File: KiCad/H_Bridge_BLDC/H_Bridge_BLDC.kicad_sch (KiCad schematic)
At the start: 32 parts, among them J1 DriveCoil, Q1 BC32740BU, Q2 TIP2955G, Q3 TIP3055G, Q4 TIP3055G, Q5 TIP2955G, Q6 BC32740BU, U1 VO615A, U4 VO615A

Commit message: First version
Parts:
- removed D1: GBU6B, Diode_THT:Diode_Bridge_Vishay_GBU, symbol Diode_Bridge:GBU6B
- added D20, D21, D22, D23: 1N5408, Diode_THT:D_DO-201AD_P15.24mm_Horizontal, symbol Diode:1N5408
- C3: footprint Capacitor_THT:CP_Radial_D25.0mm_P10.00mm_SnapIn -> Capacitor_THT:CP_Radial_D10.0mm_P5.00mm; symbol Components:470-uF-250V-PK2E471MND2535 -> Components:470-uF-50V-ECA-1HM471; Digikey https://www.digikey.nl/short/3fbd49pc -> https://www.digikey.nl/short/nq94djb8
- C4, C5, C6: footprint footprints:CP_Radial_D25.0mm_P10.00mm_and_5mm -> Capacitor_THT:CP_Radial_D10.0mm_P5.00mm; symbol Components:470-uF-250V-PK2E471MND2535 -> Components:470-uF-50V-ECA-1HM471; Digikey https://www.digikey.nl/short/3fbd49pc -> https://www.digikey.nl/short/nq94djb8
- Q1, Q6: value BC32740BU -> 2N5401; symbol Components:BC32740BU -> Components:2N5401; Digikey https://www.digikey.nl/short/7rn09zn2 -> https://www.digikey.nl/short/hrnt4cb2
- Q2, Q5: value TIP2955G -> BDW94C; footprint Package_TO_SOT_THT:TO-247-3_Vertical -> Package_TO_SOT_THT:TO-220-3_Vertical; symbol Transistor_BJT:TIP2955G -> Transistor_BJT:BDW94C
- Q3, Q4: value TIP3055G -> BDW93C; footprint Package_TO_SOT_THT:TO-247-3_Vertical -> Package_TO_SOT_THT:TO-220-3_Vertical; symbol Transistor_BJT:TIP3055G -> Transistor_BJT:BDW93C
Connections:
- net BR+: now also D21.1 (K), D23.1 (K)
- net C1: now also D22.1 (K), D23.2 (A)
- net C2: now also D20.1 (K), D21.2 (A)
- net GND: now also D20.2 (A), D22.2 (A)
- net at R3.1: now also Q1.1 (E); no longer Q1.3 (E)
- net at R8.2: now also Q6.1 (E); no longer Q6.3 (E)
- net at Q4.1 (B), R6.1: now also Q6.3 (C); no longer Q6.1 (C)
- net at Q3.1 (B), R5.2: now also Q1.3 (C); no longer Q1.1 (C)

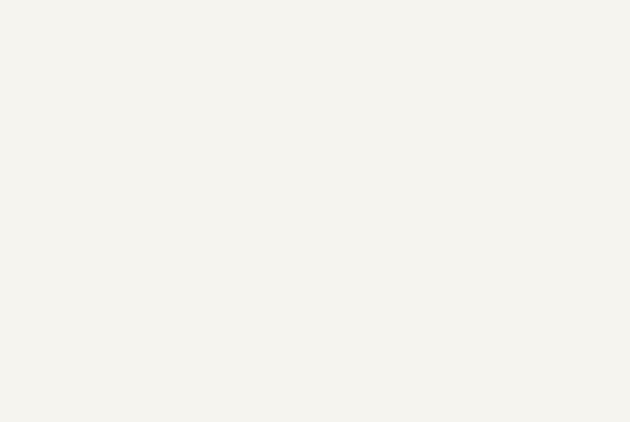
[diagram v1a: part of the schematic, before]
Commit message: Added mounting holes
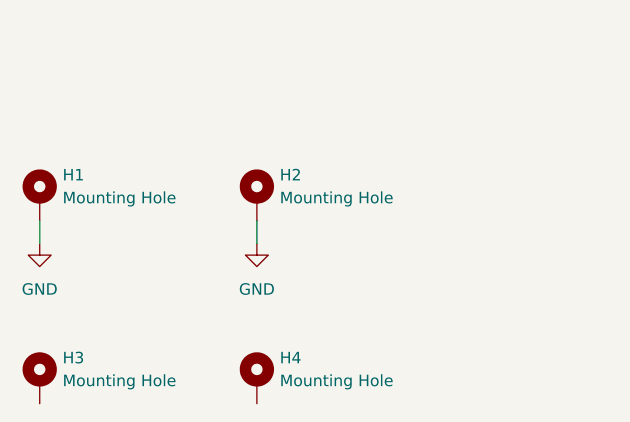
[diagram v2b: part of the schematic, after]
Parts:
- added H1, H2, H3, H4: Mounting Hole, MountingHole:MountingHole_3.2mm_M3_DIN965_Pad, symbol Mechanical:MountingHole_Pad
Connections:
- net GND: now also H1.1, H2.1

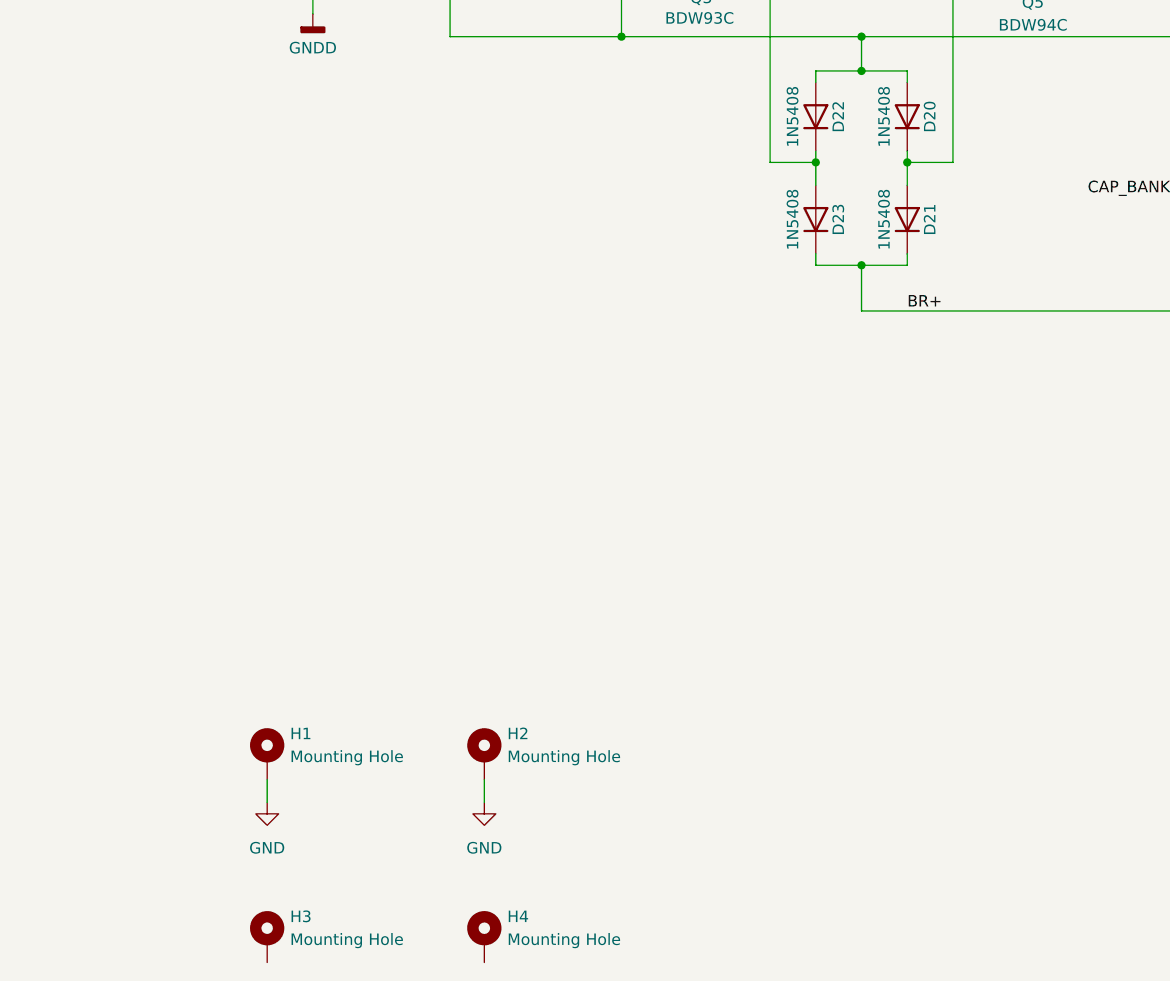
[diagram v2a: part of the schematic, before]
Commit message: Added some connectors for expermental area
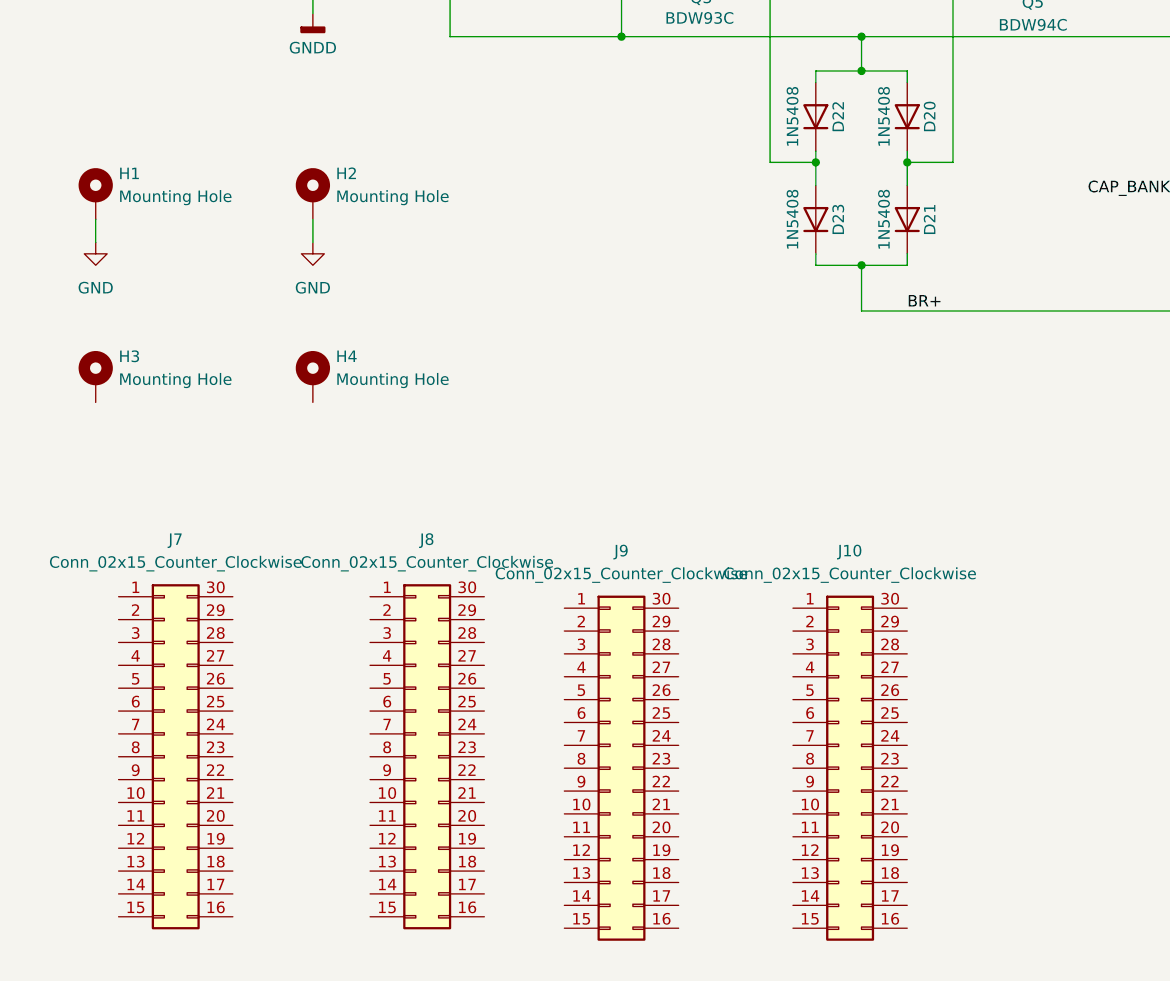
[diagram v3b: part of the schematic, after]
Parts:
- added J10, J7, J8, J9: Conn_02x15_Counter_Clockwise, Connector_PinHeader_2.54mm:PinHeader_2x15_P2.54mm_Vertical, symbol Connector_Generic:Conn_02x15_Counter_Clockwise
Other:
- moved on the sheet: H1, H2, H3, H4

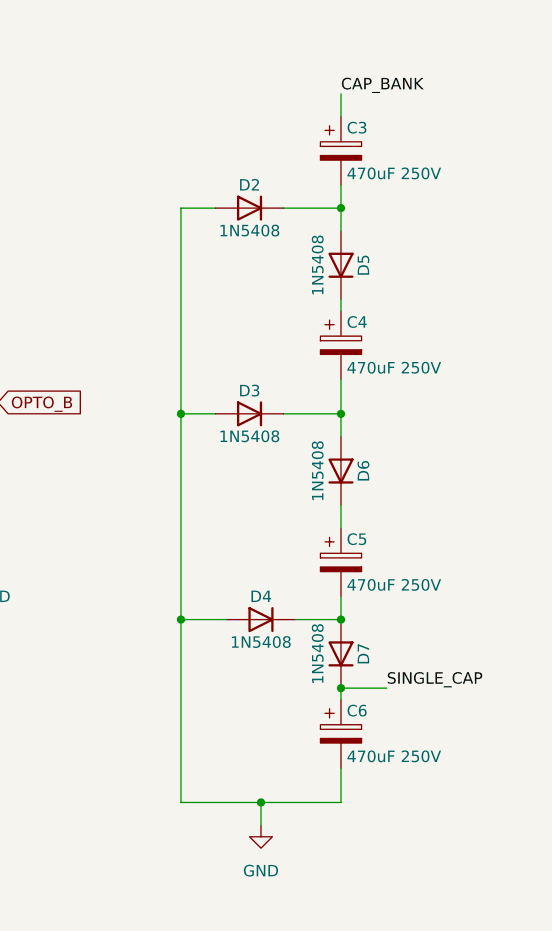
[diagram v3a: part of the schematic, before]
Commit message: Added BOM and changed some parts (same footprint)
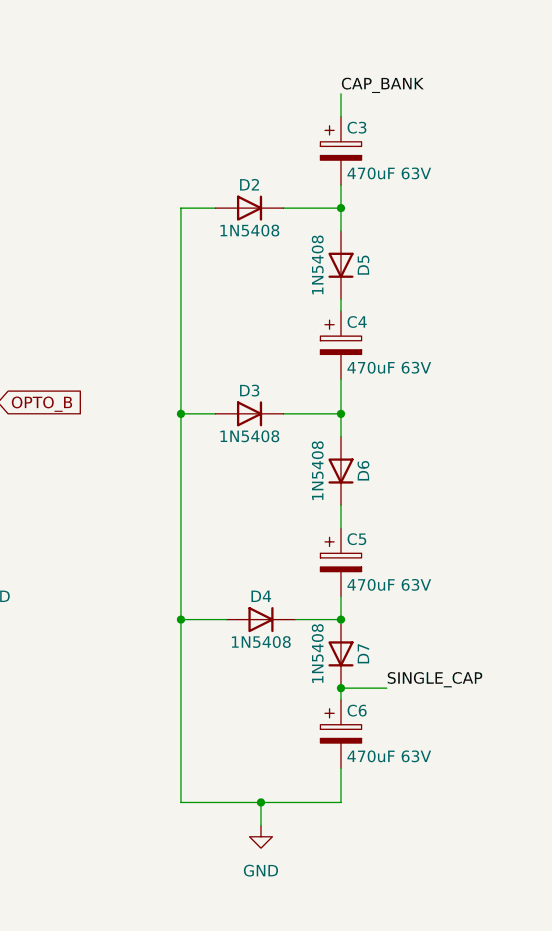
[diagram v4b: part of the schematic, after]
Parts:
- C3, C4, C5, C6: value 470uF 250V -> 470uF 63V; symbol Components:470-uF-50V-ECA-1HM471 -> Components:470-uF-63V-ESK477M063AL4EA; Digikey https://www.digikey.nl/short/nq94djb8 -> https://www.digikey.nl/short/2thtjq03
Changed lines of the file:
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@@
 	)
 	(symbol
-		(lib_id "Components:470-uF-50V-ECA-1HM471")
+		(lib_id "Components:470-uF-63V-ESK477M063AL4EA")
 		(at 220.98 54.61 0)
 		(unit 1)
@@
 			)
 		)
-		(property "Value" "470uF 250V"
+		(property "Value" "470uF 63V"
 			(at 221.615 57.15 0)
 			(effects
@@
 			)
 		)
-		(property "Datasheet" "https://mm.digikey.com/Volume0/opasdata/d220001/medias/docus/2452/ECA-xxM%20Series%2CTypeA.pdf"
+		(property "Datasheet" "https://search.kemet.com/download/datasheet/ESK477M063AL4EA"
 			(at 220.98 54.61 0)
 			(effects
@@
 			)
 		)
-		(property "Digikey" "https://www.digikey.nl/short/nq94djb8"
+		(property "Digikey" "https://www.digikey.nl/short/2thtjq03"
 			(at 220.98 54.61 0)
 			(effects
@@
 	)
 	(symbol
-		(lib_id "Components:470-uF-50V-ECA-1HM471")
+		(lib_id "Components:470-uF-63V-ESK477M063AL4EA")
 		(at 220.98 78.74 0)
 		(unit 1)
@@
 			)
 		)
-		(property "Value" "470uF 250V"
+		(property "Value" "470uF 63V"
 			(at 221.615 81.28 0)
 			(effects
@@
 			)
 		)
-		(property "Datasheet" "https://mm.digikey.com/Volume0/opasdata/d220001/medias/docus/2452/ECA-xxM%20Series%2CTypeA.pdf"
+		(property "Datasheet" "https://search.kemet.com/download/datasheet/ESK477M063AL4EA"
 			(at 220.98 78.74 0)
 			(effects
@@
 			)
 		)
-		(property "Digikey" "https://www.digikey.nl/short/nq94djb8"
+		(property "Digikey" "https://www.digikey.nl/short/2thtjq03"
 			(at 220.98 78.74 0)
 			(effects
@@
 	)
 	(symbol
-		(lib_id "Components:470-uF-50V-ECA-1HM471")
+		(lib_id "Components:470-uF-63V-ESK477M063AL4EA")
 		(at 220.98 97.79 0)
 		(unit 1)
@@
 			)
 		)
-		(property "Value" "470uF 250V"
+		(property "Value" "470uF 63V"
 			(at 221.615 100.33 0)
 			(effects
@@
 			)
 		)
-		(property "Datasheet" "https://mm.digikey.com/Volume0/opasdata/d220001/medias/docus/2452/ECA-xxM%20Series%2CTypeA.pdf"
+		(property "Datasheet" "https://search.kemet.com/download/datasheet/ESK477M063AL4EA"
 			(at 220.98 97.79 0)
 			(effects
@@
 			)
 		)
-		(property "Digikey" "https://www.digikey.nl/short/nq94djb8"
+		(property "Digikey" "https://www.digikey.nl/short/2thtjq03"
 			(at 220.98 97.79 0)
 			(effects
@@
 	)
 	(symbol
-		(lib_id "Components:470-uF-50V-ECA-1HM471")
+		(lib_id "Components:470-uF-63V-ESK477M063AL4EA")
 		(at 220.98 33.02 0)
 		(unit 1)
@@
 			)
 		)
-		(property "Value" "470uF 250V"
+		(property "Value" "470uF 63V"
 			(at 221.615 35.56 0)
 			(effects
@@
 			)
 		)
-		(property "Datasheet" "https://mm.digikey.com/Volume0/opasdata/d220001/medias/docus/2452/ECA-xxM%20Series%2CTypeA.pdf"
+		(property "Datasheet" "https://search.kemet.com/download/datasheet/ESK477M063AL4EA"
 			(at 220.98 33.02 0)
 			(effects
@@
 			)
 		)
-		(property "Digikey" "https://www.digikey.nl/short/nq94djb8"
+		(property "Digikey" "https://www.digikey.nl/short/2thtjq03"
 			(at 220.98 33.02 0)
 			(effects

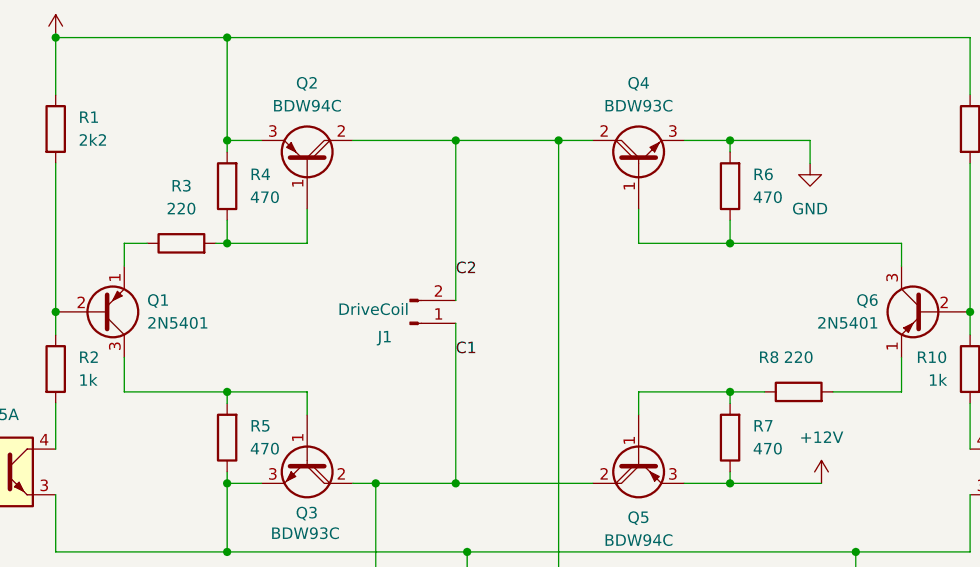
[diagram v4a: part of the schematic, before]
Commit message: Changed a few values and completed BOM.
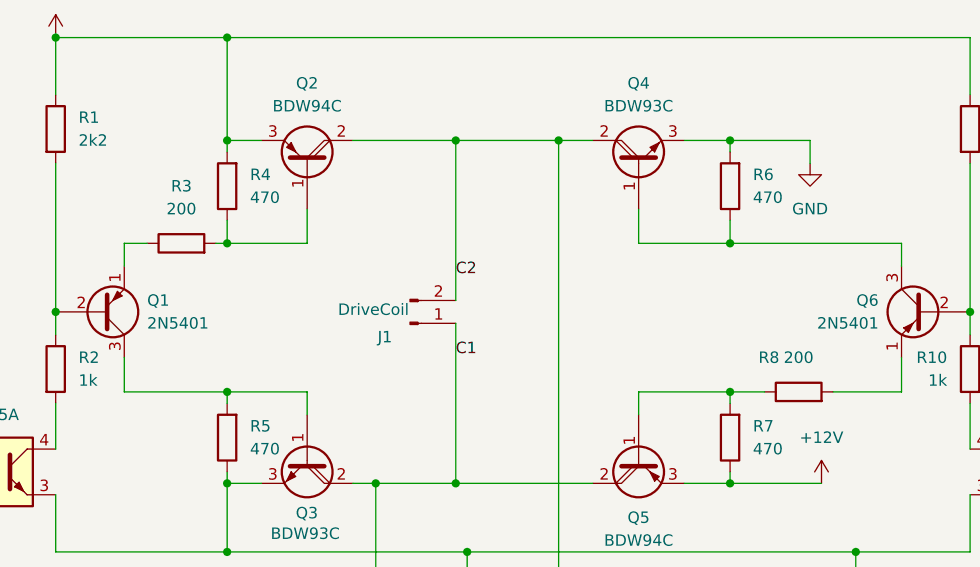
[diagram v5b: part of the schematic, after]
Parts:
- R3, R8: value 220 -> 200
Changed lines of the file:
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@@
 			)
 		)
-		(property "Value" "220"
+		(property "Value" "200"
 			(at 78.74 43.18 90)
 			(effects
@@
 			)
 		)
-		(property "Value" "220"
+		(property "Value" "200"
 			(at 147.32 59.69 90)
 			(effects

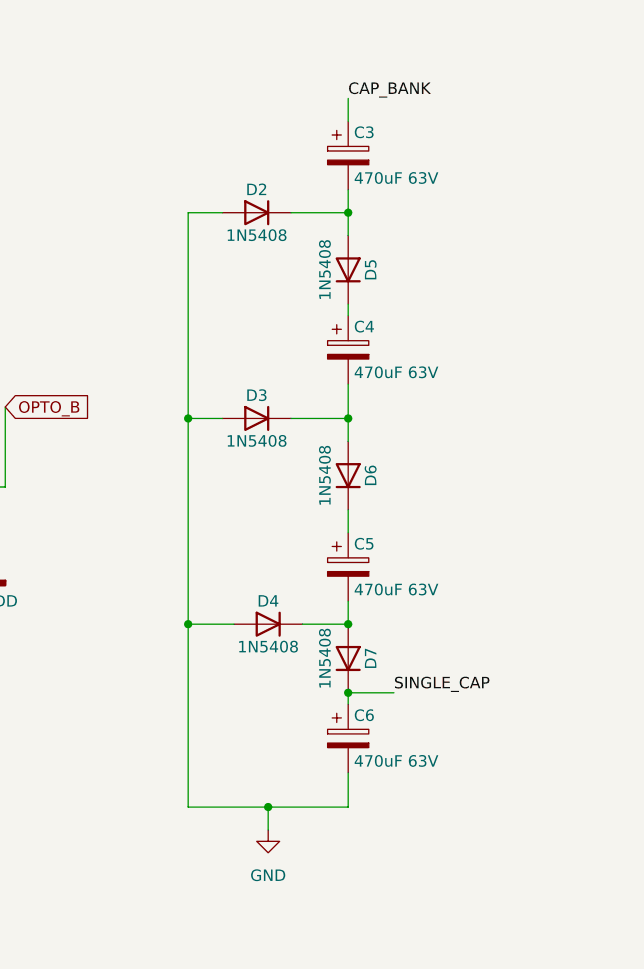
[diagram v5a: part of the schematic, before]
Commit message: Corrected schematic with components that need to be manually added.
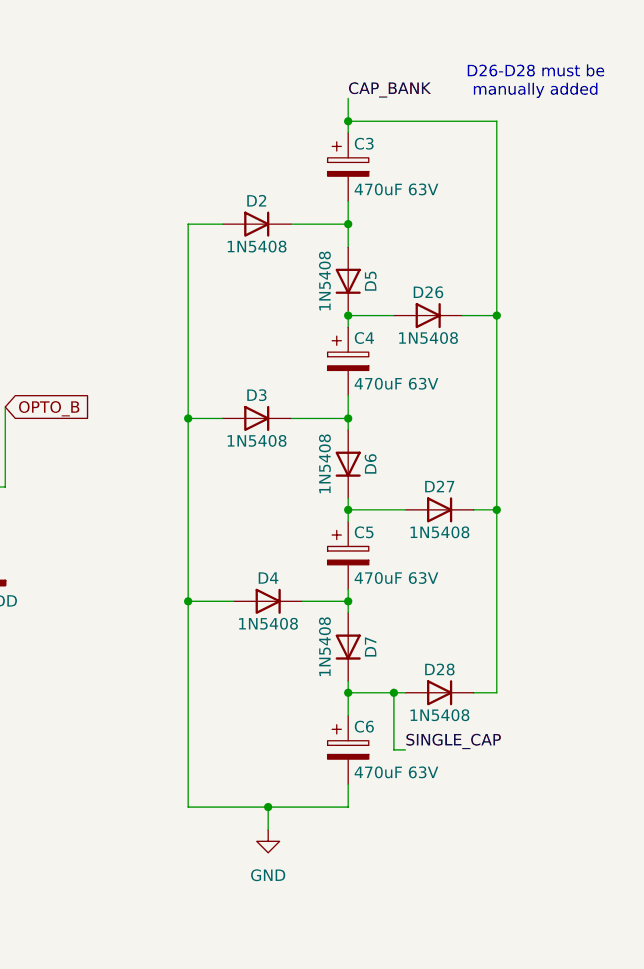
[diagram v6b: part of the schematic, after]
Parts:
- added D26, D27, D28: 1N5408, Diode_THT:D_DO-201AD_P15.24mm_Horizontal, symbol Diode:1N5408
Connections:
- net CAP_BANK: now also D26.1 (K), D27.1 (K), D28.1 (K)
- net SINGLE_CAP: now also D28.2 (A)
- net at C5.1, D6.1 (K): now also D27.2 (A)
- net at C4.1, D5.1 (K): now also D26.2 (A)
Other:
- note added: "D26-D28 must be manually added"
- moved on the sheet: C3, C4, C5, C6, D2, D4, D5, D6, D7
